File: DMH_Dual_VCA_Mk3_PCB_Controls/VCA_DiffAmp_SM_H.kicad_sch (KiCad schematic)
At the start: 18 parts, among them Q1 BC548, Q2 BC548, U2 TL072

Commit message: Experimenting with VCA design blocks
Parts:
- added J10: Conn_02x03_Odd_Even, Connector_PinHeader_2.54mm:PinHeader_2x03_P2.54mm_Horizontal, symbol Connector_Generic:Conn_02x03_Odd_Even
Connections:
- net +12V: now also J10.1 (Pin_1)
- net -12V: now also J10.3 (Pin_3)
- net GND: now also J10.5 (Pin_5)
- net CV Mix In renamed CV_Mix_In
- net CV_Mix_In: now also J10.2 (Pin_2)
- net Signal In renamed Signal_In
- net Signal_In: now also J10.4 (Pin_4)
- net Signal Out renamed Signal_Out
- net Signal_Out: now also J10.6 (Pin_6)

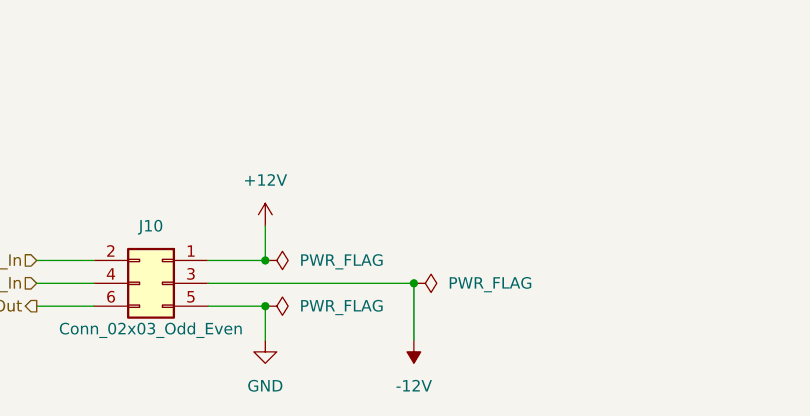
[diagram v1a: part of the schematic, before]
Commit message: Redesigned schematic layout
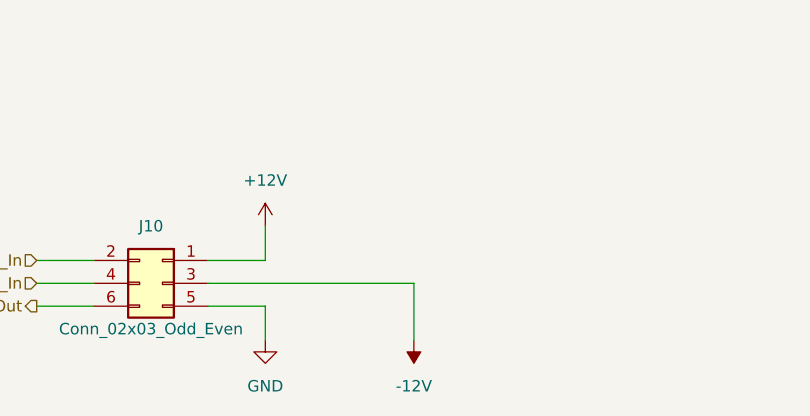
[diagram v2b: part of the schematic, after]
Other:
- company: (none) -> DMH Instruments
